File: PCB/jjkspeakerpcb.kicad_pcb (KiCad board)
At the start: 2 copper layers, 99.3 x 99.3 mm, 19 parts, among them J1 TFT 8PIN, SW1 UP, SW2 DOWN, SW3 TIME SET, SW4 CLOCK SET, SW5 SNOOZE, SW6 ALARM ON, U1 XIAO ESP32-C3

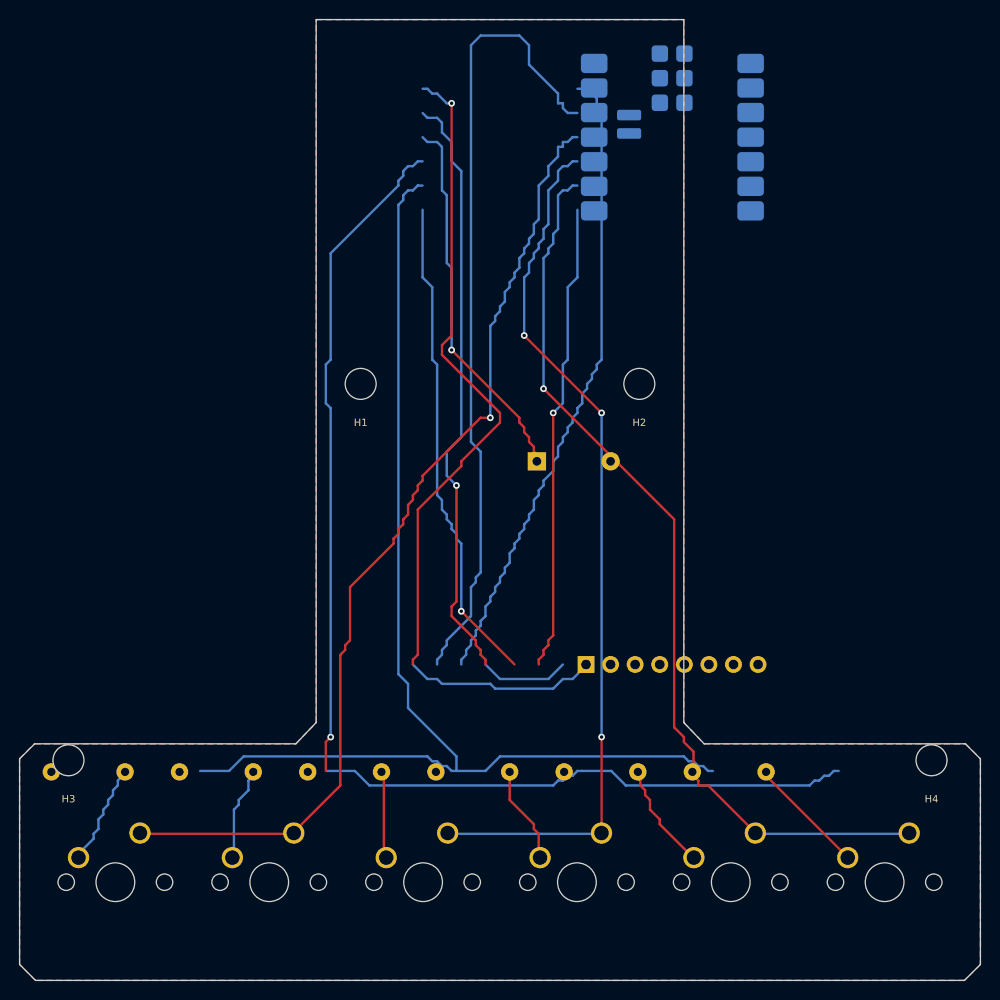
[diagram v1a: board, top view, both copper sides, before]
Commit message: Regenerate PCB and schematic using KiCad backside coordinates
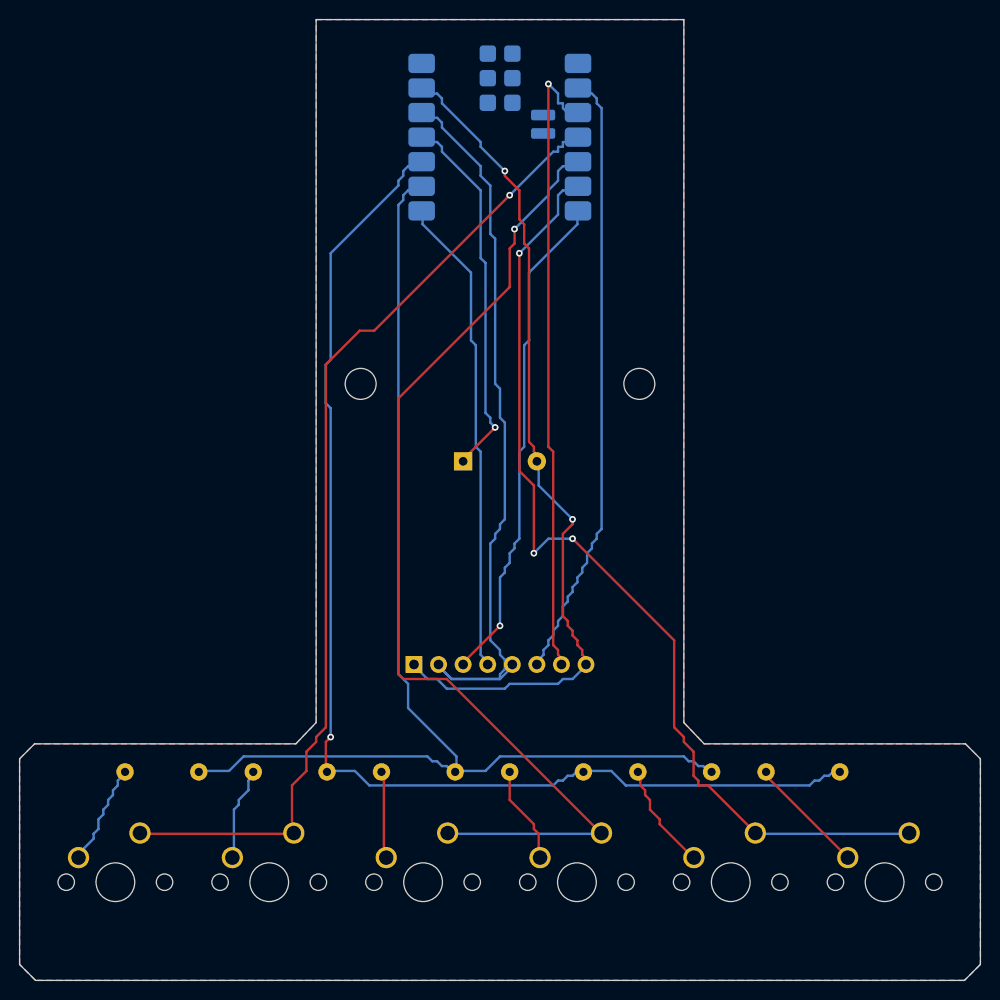
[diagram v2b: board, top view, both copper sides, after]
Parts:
- removed the H1 at (35.6, 38.0)
- removed H3, H4: M3, GGK:MountingHole_3.2
- added BZ1: 3.3V PIEZO, GGK:Piezo_P12_P7.62, B.Cu at (46.2, 46.0)
- H1: renamed from BZ1; value 3.3V PIEZO -> M3; footprint GGK:Piezo_P12_P7.62 -> GGK:MountingHole_3.2; moved to F.Cu
- moved H1 19.9 mm to (35.6, 38.0)
- moved J1 17.8 mm to (41.1, 67.0)
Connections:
- net 3V3 renamed /3V3
- net COL_BOTTOM renamed /COL_BOTTOM
- net COL_MIDDLE renamed /COL_MIDDLE
- net COL_TOP renamed /COL_TOP
- net DISP_CS renamed /DISP_CS
- net DISP_DC renamed /DISP_DC
- net DISP_MOSI renamed /DISP_MOSI
- net DISP_SCK renamed /DISP_SCK
- net K1 renamed /K1
- net K2 renamed /K2
- net K3 renamed /K3
- net K4 renamed /K4
- net K5 renamed /K5
- net K6 renamed /K6
- net ROW_LEFT renamed /ROW_LEFT
- net ROW_RIGHT renamed /ROW_RIGHT
- J1 pad 1: GND -> /GND
- J1 pad 8: GND -> /GND
- U1 pad 11: PIEZO -> /PIEZO
- U1 pad 13: GND -> /GND
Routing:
- net GND: track 88.3 -> 0.00 mm, vias 1 -> 0
- net /GND: track 0.00 -> 88.0 mm, vias 0 -> 2
- net PIEZO: track 39.1 -> 0.00 mm, vias 1 -> 0
- net /PIEZO: track 0.00 -> 38.6 mm, vias 0 -> 1
- net /DISP_CS: track 83.1 -> 65.7 mm, vias 0 -> 1
- net /COL_MIDDLE: track 91.7 -> 105.1 mm, vias 3 -> 1
- net /3V3: track 71.2 -> 80.4 mm, vias 1 -> 0
- net /COL_BOTTOM: track 94.7 -> 101.3 mm, vias 1 -> 3
- net /DISP_SCK: track 48.7 -> 52.0 mm
- net /DISP_DC: track 67.1 -> 63.8 mm
- net /DISP_MOSI: track 50.9 -> 49.7 mm, vias 1 -> 0
- net /COL_TOP: track 101.2 -> 101.8 mm
- added copper zone on B.Cu, net /GND
- added copper zone on F.Cu, net /GND
- removed copper zone on B.Cu, net GND
- removed copper zone on F.Cu, net GND
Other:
- board text added: "6 KEY MATRIX / PORTRAIT TFT"
- board text added: "GGK ALARM REV D"
- board text removed: "6 KEY MATRIX // TFT ON FRONT"
- board text removed: "GGK ALARM R2"
